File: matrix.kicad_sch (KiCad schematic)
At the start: 42 parts, among them SW10 7/home, SW11 8/up, SW12 9/pgup, SW13 +, SW14 4/left, SW15 5, SW16 6/right, SW18 1/end, SW19 2/down, SW2 ESC, SW20 3/pgdn, SW22 0/insert, SW23 ./delete, SW24 ENTER, SW3 TAB, SW4 BACKSPACE, SW5 FN, SW6 NUM_LOCK, SW7 /, SW8 *, SW9 -

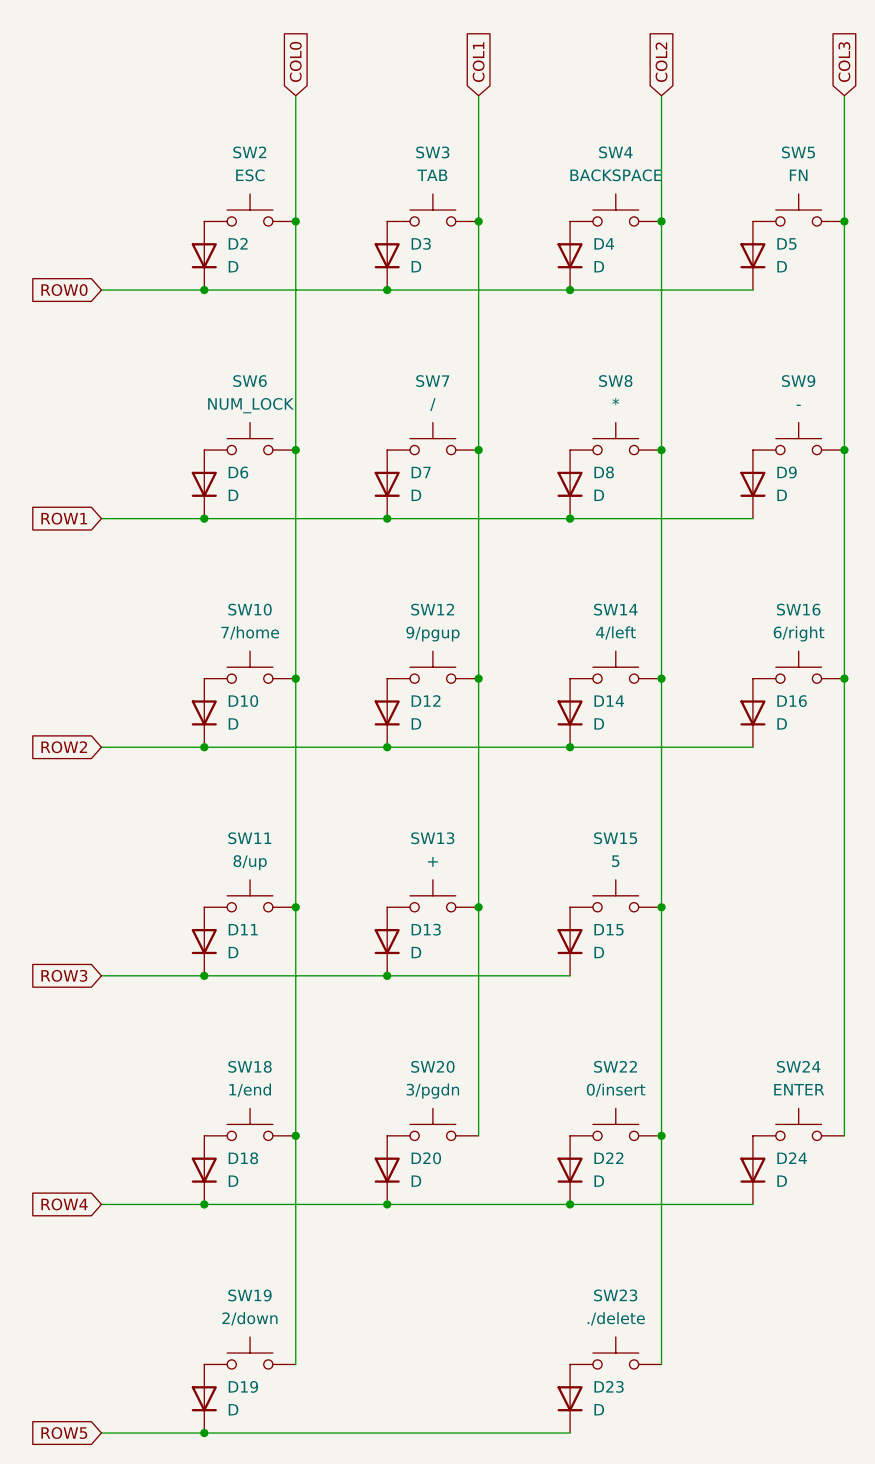
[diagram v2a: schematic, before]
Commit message: Correct PCB footprints
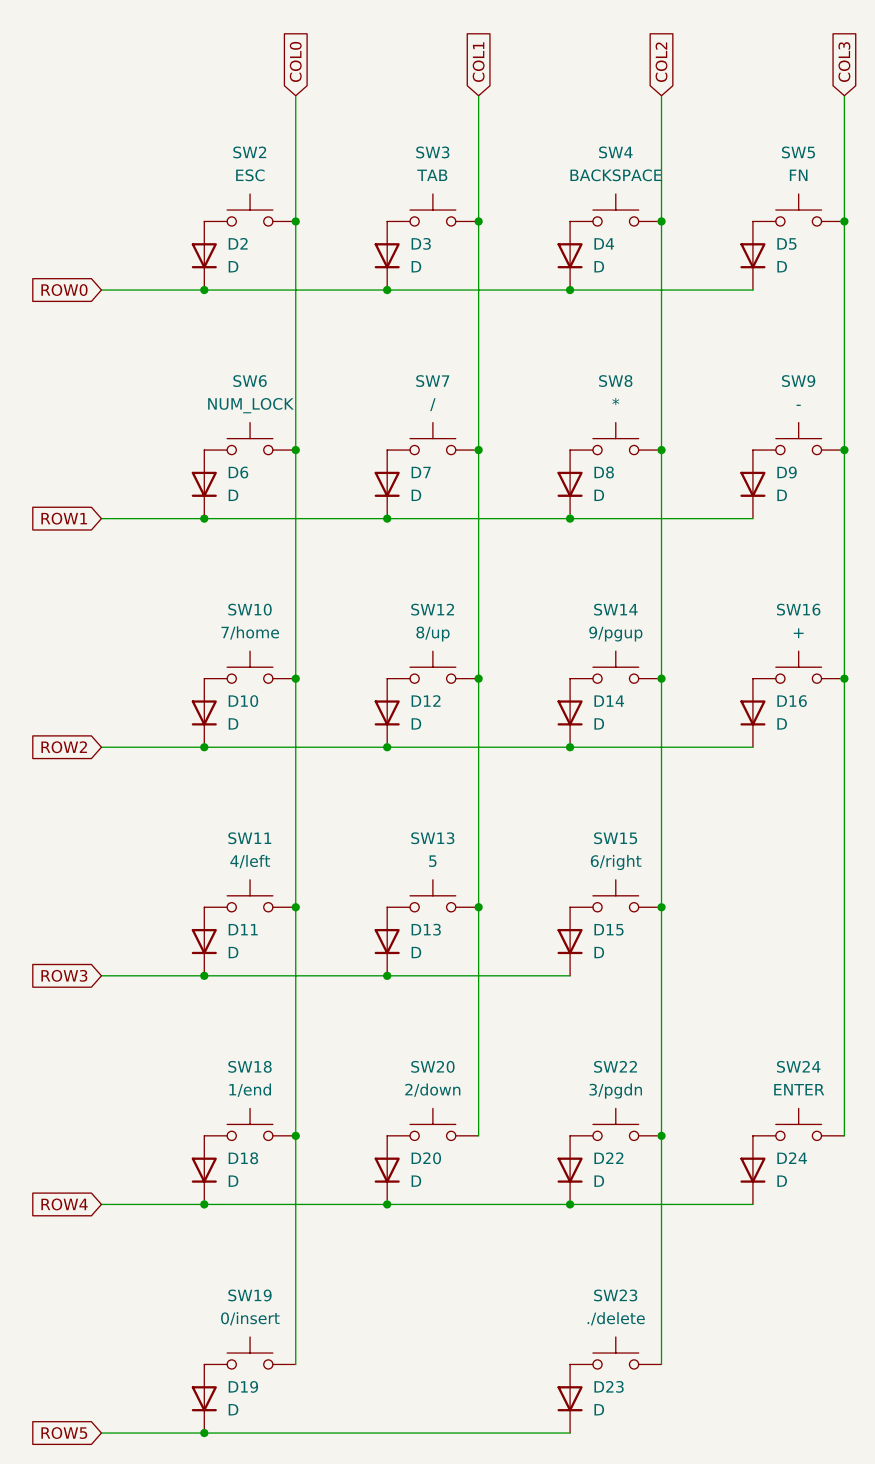
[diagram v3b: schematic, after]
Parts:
- SW11: value 8/up -> 4/left
- SW12: value 9/pgup -> 8/up
- SW13: value + -> 5; footprint Alps_Only:ALPS-2U -> Alps_Only:ALPS-1U
- SW14: value 4/left -> 9/pgup
- SW15: value 5 -> 6/right
- SW16: value 6/right -> +; footprint Alps_Only:ALPS-1U -> Alps_Only:ALPS-2U
- SW19: value 2/down -> 0/insert; footprint Alps_Only:ALPS-1U -> Alps_Only:ALPS-2U
- SW20: value 3/pgdn -> 2/down
- SW22: value 0/insert -> 3/pgdn; footprint Alps_Only:ALPS-2U -> Alps_Only:ALPS-1U
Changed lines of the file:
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@@
 			)
 		)
-		(property "Value" "8/up"
+		(property "Value" "4/left"
 			(at 73.66 113.03 0)
 			(effects
@@
 			)
 		)
-		(property "Value" "3/pgdn"
+		(property "Value" "2/down"
 			(at 93.98 138.43 0)
 			(effects
@@
 			)
 		)
-		(property "Value" "6/right"
+		(property "Value" "+"
 			(at 134.62 87.63 0)
 			(effects
@@
 			)
 		)
-		(property "Footprint" "Alps_Only:ALPS-1U"
+		(property "Footprint" "Alps_Only:ALPS-2U"
 			(at 134.62 87.63 0)
 			(effects
@@
 			)
 		)
-		(property "Value" "9/pgup"
+		(property "Value" "8/up"
 			(at 93.98 87.63 0)
 			(effects
@@
 			)
 		)
-		(property "Value" "2/down"
+		(property "Value" "0/insert"
 			(at 73.66 163.83 0)
 			(effects
@@
 			)
 		)
-		(property "Footprint" "Alps_Only:ALPS-1U"
+		(property "Footprint" "Alps_Only:ALPS-2U"
 			(at 73.66 163.83 0)
 			(effects
@@
 			)
 		)
-		(property "Value" "+"
+		(property "Value" "5"
 			(at 93.98 113.03 0)
 			(effects
@@
 			)
 		)
-		(property "Footprint" "Alps_Only:ALPS-2U"
+		(property "Footprint" "Alps_Only:ALPS-1U"
 			(at 93.98 113.03 0)
 			(effects
@@
 			)
 		)
-		(property "Value" "0/insert"
+		(property "Value" "3/pgdn"
 			(at 114.3 138.43 0)
 			(effects
@@
 			)
 		)
-		(property "Footprint" "Alps_Only:ALPS-2U"
+		(property "Footprint" "Alps_Only:ALPS-1U"
 			(at 114.3 138.43 0)
 			(effects
@@
 			)
 		)
-		(property "Value" "4/left"
+		(property "Value" "9/pgup"
 			(at 114.3 87.63 0)
 			(effects
@@
 			)
 		)
-		(property "Value" "5"
+		(property "Value" "6/right"
 			(at 114.3 113.03 0)
 			(effects
